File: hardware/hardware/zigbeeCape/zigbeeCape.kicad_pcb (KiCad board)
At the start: 4 copper layers, 63.5 x 54.6 mm, 80 parts, among them J1 Conn_ARM_JTAG_SWD_10, SW1 SW_MEC_5E, SW2 SW_MEC_5E, SW3 SW_MEC_5E, SW4 SW_MEC_5E, SW5 SW_MEC_5E, U1 CC1352R, U2 0.8Ghz_and_2.4GHz_Filter, U3 SMA_Antenna, U4 BeagleBone_P8, U5 BeagleBone_P9, Y1 32.768kHz, Y2 48MHz

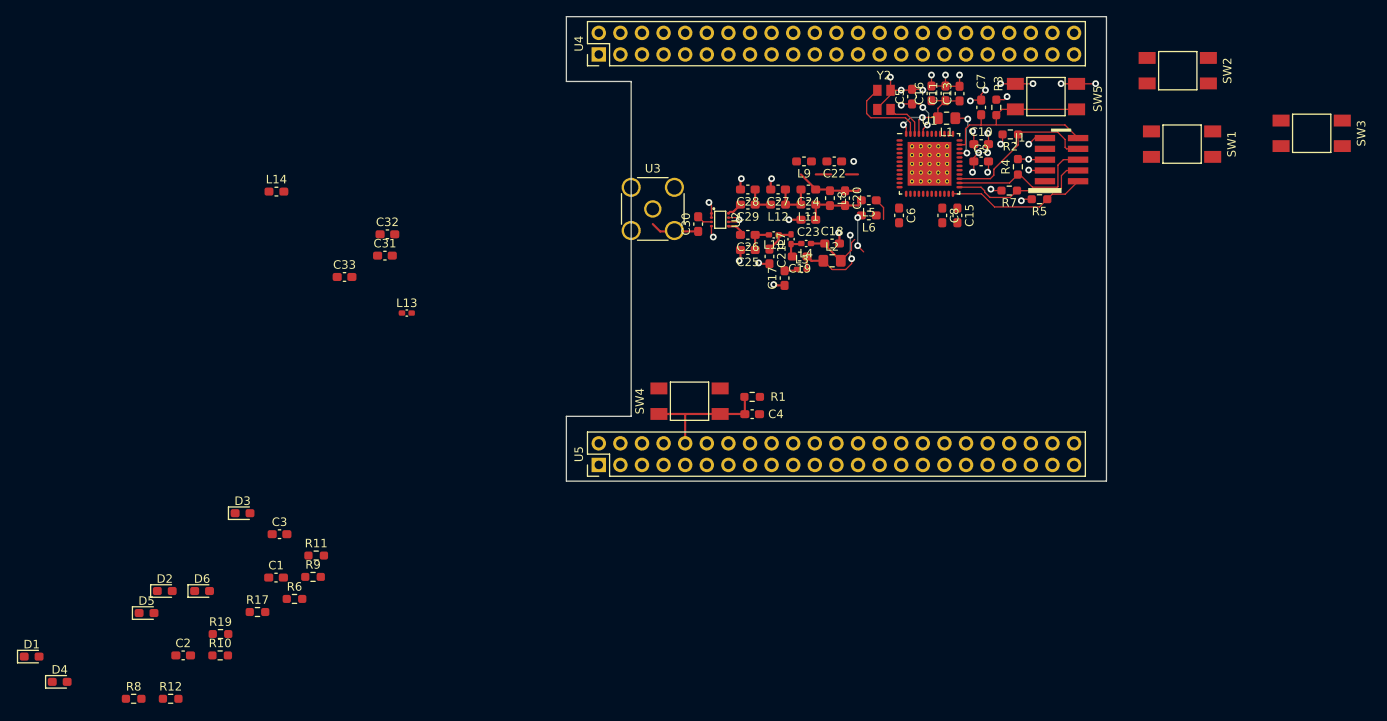
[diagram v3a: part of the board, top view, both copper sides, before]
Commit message: Buttons, most LEDs are done
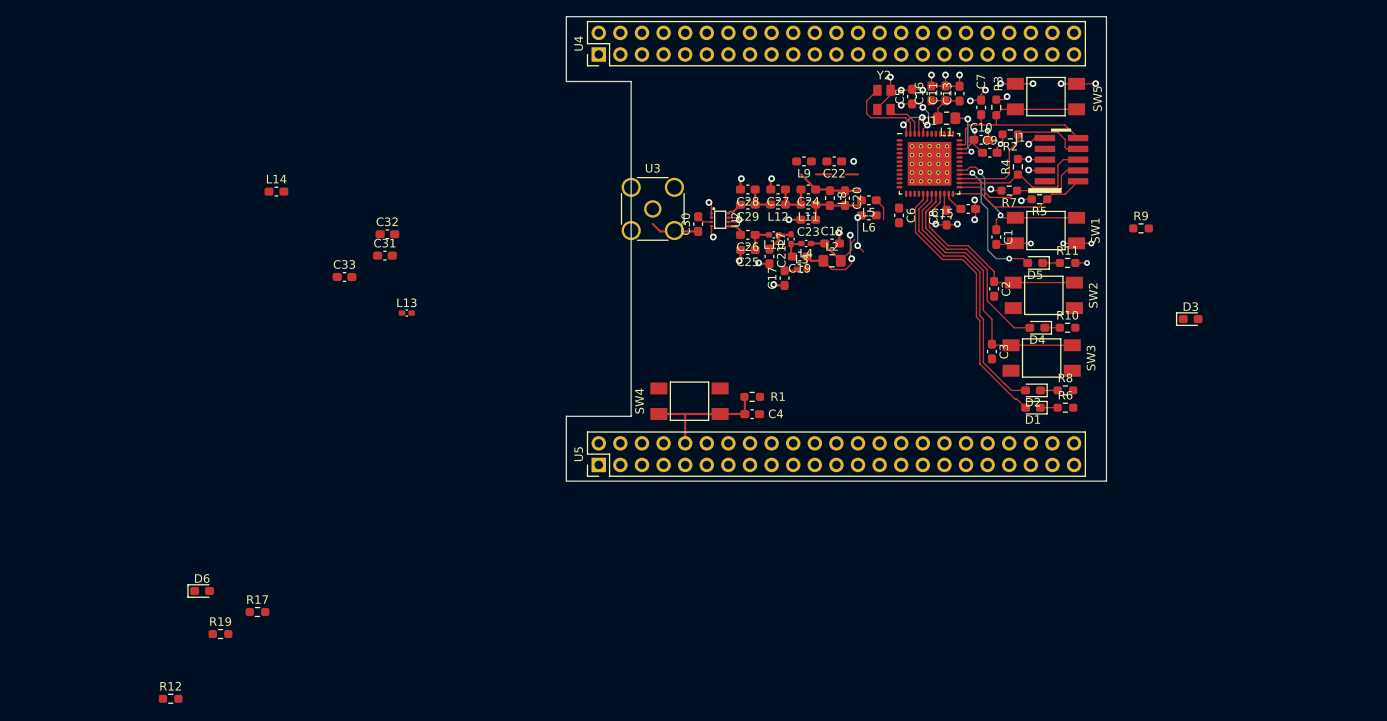
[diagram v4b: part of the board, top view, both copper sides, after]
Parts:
- moved D4 122.3 mm to (55.4, -18.0), turned to 180 degrees
- moved D1 121.3 mm to (54.9, -8.64), turned to 180 degrees
- moved R8 115.4 mm to (58.7, -10.7)
- moved D3 113.8 mm to (73.4, -19.1)
- moved D5 112.3 mm to (55.1, -25.7), turned to 180 degrees
- moved R10 106.8 mm to (58.9, -18.0)
- moved R9 105.6 mm to (67.6, -29.7)
- moved D2 104.8 mm to (54.9, -10.7), turned to 180 degrees
- moved C2 104.6 mm to (50.3, -22.6), turned to 270 degrees
- moved R11 94.8 mm to (58.9, -25.7)
- moved C1 93.7 mm to (50.5, -28.7), turned to 270 degrees
- moved R6 93.4 mm to (58.7, -8.64)
- moved C3 86.5 mm to (50.0, -15.2), turned to 270 degrees
- moved SW3 41.3 mm to (55.9, -14.5)
- moved SW2 30.8 mm to (56.1, -21.8)
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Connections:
- C4 pad 1: /BeagleBone_Headers/BeagleBone_Reset -> Net-(C4-Pad1)
- R1 pad 2: /BeagleBone_Headers/BeagleBone_Reset -> Net-(C4-Pad1)
- R17 pad 2: I2C2_SDA -> I2C2_SCL
- R19 pad 2: I2C2_SCL -> I2C2_SDA
- SW4 pad 3: /BeagleBone_Headers/BeagleBone_Reset -> Net-(C4-Pad1)
- SW4 pad 4: /BeagleBone_Headers/BeagleBone_Reset -> Net-(C4-Pad1)
- U1 pad 15: Net-(U1-Pad15) -> I2C2_SCL
- U1 pad 16: Net-(U1-Pad16) -> I2C2_SDA
- U1 pad 17: Net-(U1-Pad17) -> Aux_1
- U1 pad 18: Net-(U1-Pad18) -> Aux_2
- U1 pad 19: Net-(U1-Pad19) -> Check_Error
- U1 pad 20: I2C2_SCL -> ZigBee_HeartBeat
- U1 pad 21: I2C2_SDA -> ZigBee_Connect
- U1 pad 28: ZigBee_Connect -> Lan_HeartBeat
- U1 pad 29: Check_Error -> Network_Connect
- U1 pad 30: ZigBee_HeartBeat -> Net-(U1-Pad30)
- U1 pad 31: Cape_HeartBeat -> Net-(U1-Pad31)
- U1 pad 32: Aux_2 -> Net-(U1-Pad32)
- U1 pad 36: Aux_1 -> Net-(U1-Pad36)
- U1 pad 37: Net-(U1-Pad37) -> Cape_HeartBeat
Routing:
- net Aux_1: track 0.00 -> 32.4 mm
- net Check_Error: track 0.00 -> 32.4 mm
- net Aux_2: track 0.00 -> 31.1 mm
- net ZigBee_Connect: track 0.00 -> 24.9 mm
- net ZigBee_HeartBeat: track 0.00 -> 23.8 mm
- net Network_Connect: track 0.00 -> 19.9 mm, vias 0 -> 2
- net Lan_HeartBeat: track 0.00 -> 16.8 mm, vias 0 -> 2
- net GND: track 58.8 -> 72.9 mm, vias 32 -> 38
- net Net-(C15-Pad1): track 0.00 -> 2.48 mm
- net Net-(D5-Pad1): track 0.00 -> 2.02 mm
- net Net-(D2-Pad1): track 0.00 -> 2.02 mm
- net Net-(D1-Pad1): track 0.00 -> 2.02 mm
- net Net-(D4-Pad1): track 0.00 -> 1.77 mm
- net +3V3: track 13.8 -> 15.0 mm, vias 7 -> 5
- net Net-(J1-Pad8): track 19.1 -> 20.1 mm
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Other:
- rule via_min_drill: 0.3 -> 0.3302
- rule via_min_size: 0.4 -> 0.6858

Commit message: Setup DRC, completed coms lines
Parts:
- moved R19 87.7 mm to (38.1, -20.6), turned to 90 degrees
- moved R17 84.6 mm to (38.1, -24.9), turned to 90 degrees
- moved C26 46.1 mm to (-23.1, -41.1)
- moved L10 46.1 mm to (-20.1, -41.1)
- moved L3 46.1 mm to (-16.8, -37.1)
- moved C17 46.1 mm to (-18.8, -36.1)
- moved C18 46.1 mm to (-13.2, -40.1)
- moved C19 46.1 mm to (-17.0, -38.6)
- moved C21 46.1 mm to (-20.6, -38.6)
- moved C22 46.1 mm to (-13.0, -49.8)
- moved C23 46.1 mm to (-16.0, -42.9)
- moved C24 46.1 mm to (-16.0, -46.5)
- moved C25 46.1 mm to (-23.1, -39.4)
- moved C27 46.1 mm to (-19.6, -46.5)
- moved C28 46.1 mm to (-23.1, -46.5)
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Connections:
- C4 pad 1: Net-(C4-Pad1) -> /BeagleBone_Headers/BeagleBone_Reset
- R1 pad 2: Net-(C4-Pad1) -> /BeagleBone_Headers/BeagleBone_Reset
- SW4 pad 3: Net-(C4-Pad1) -> /BeagleBone_Headers/BeagleBone_Reset
- SW4 pad 4: Net-(C4-Pad1) -> /BeagleBone_Headers/BeagleBone_Reset
- U1 pad 10: SPI_MISO -> I2C2_SDA
- U1 pad 11: SPI_MOSI -> I2C2_SCL
- U1 pad 12: SPI_CS -> SPI_CLK
- U1 pad 14: SPI_CLK -> SPI_MISO
- U1 pad 15: I2C2_SCL -> UART_TX
- U1 pad 16: I2C2_SDA -> UART_RX
- U1 pad 31: Net-(U1-Pad31) -> Cape_HeartBeat
- U1 pad 37: Cape_HeartBeat -> Net-(U1-Pad37)
- U1 pad 8: UART_RX -> SPI_MOSI
- U1 pad 9: UART_TX -> SPI_CS
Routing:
- net I2C2_SCL: track 0.00 -> 43.6 mm
- net SPI_CS: track 0.00 -> 41.2 mm
- net I2C2_SDA: track 0.00 -> 39.6 mm
- net SPI_MOSI: track 0.00 -> 39.2 mm
- net GND: track 72.9 -> 112.1 mm, vias 38 -> 62
- net SPI_CLK: track 0.00 -> 37.8 mm
- net SPI_MISO: track 0.00 -> 36.5 mm
- net UART_TX: track 0.00 -> 33.2 mm
- net UART_RX: track 0.00 -> 32.3 mm
- net Cape_HeartBeat: track 0.00 -> 9.56 mm, vias 0 -> 2
- net +3V3: track 15.0 -> 23.1 mm, vias 5 -> 10
- net Net-(C14-Pad1): track 0.00 -> 6.54 mm
- net Net-(C12-Pad1): track 0.00 -> 6.02 mm
- net Net-(D3-Pad1): track 0.00 -> 2.78 mm
- net Net-(C15-Pad1): track 2.48 -> 3.44 mm
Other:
- net class Default: clearance 0.254 -> 0.1524
- rule trace_clearance: 0.254 -> 0.1524

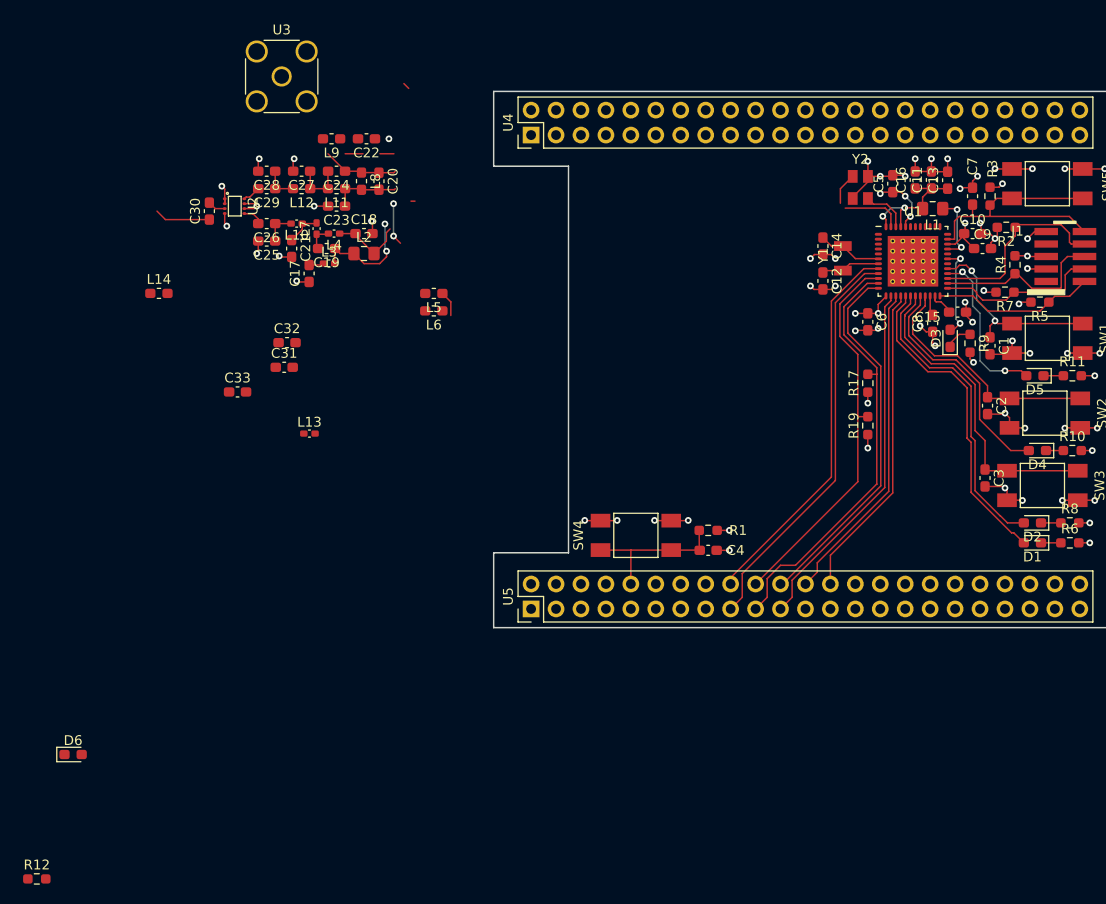
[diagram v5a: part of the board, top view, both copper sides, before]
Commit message: Finished ZigBee circuit, Removed PCB antenna
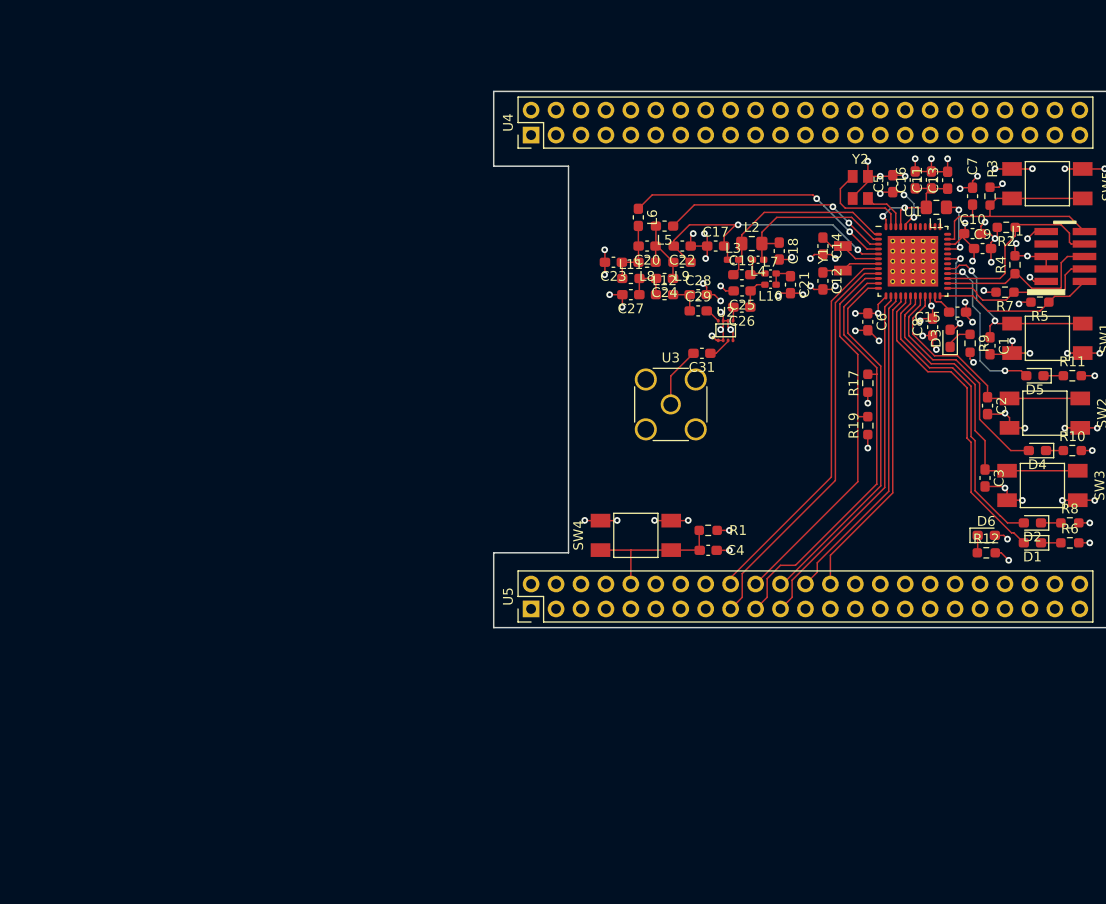
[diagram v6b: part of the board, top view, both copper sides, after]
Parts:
- removed C30, C32: DNM, Capacitor_SMD:C_0603_1608Metric_Pad1.08x0.95mm_HandSolder
- removed C33: 5.6pF, Capacitor_SMD:C_0603_1608Metric_Pad1.08x0.95mm_HandSolder
- removed L13: 3.3nH, Inductor_SMD:L_0402_1005Metric_Pad0.77x0.64mm_HandSolder
- removed L14: DNM, Inductor_SMD:L_0603_1608Metric_Pad1.05x0.95mm_HandSolder
- moved R12 102.2 mm to (50.2, -7.62)
- moved D6 95.6 mm to (50.2, -9.40)
- moved U3 51.8 mm to (18.0, -22.7)
- moved U2 51.6 mm to (23.6, -30.2), turned to 0 degrees
- moved C21 50.9 mm to (30.2, -34.9)
- moved C26 49.1 mm to (25.3, -32.6)
- moved C25 48.7 mm to (25.3, -34.3)
- moved L10 48.7 mm to (28.2, -34.9)
- moved L7 46.5 mm to (28.2, -36.1), turned to 0 degrees
- moved C28 45.7 mm to (20.8, -33.9), turned to 0 degrees
- moved C29 45.7 mm to (20.8, -32.3), turned to 0 degrees
- moved L4 43.3 mm to (26.9, -37.5)
- moved C31 42.6 mm to (21.2, -27.9), turned to 180 degrees
- moved C19 42.4 mm to (25.3, -35.9), turned to 0 degrees
- moved C18 42.3 mm to (29.1, -38.4), turned to 270 degrees
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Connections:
- C31 pad 2: Net-(C30-Pad2) -> Net-(C31-Pad2)
- U2 pad 3: Net-(C30-Pad2) -> Net-(C31-Pad1)
- U3 pad 1: Net-(C30-Pad1) -> Net-(C31-Pad2)
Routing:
- net /ZigBeeFiltering/SUB-1_GHZ_RF_N: track 0.41 -> 27.3 mm, vias 0 -> 2
- net /ZigBeeFiltering/RX_TX: track 3.34 -> 30.1 mm, vias 0 -> 2
- net /ZigBeeFiltering/SUB-1_GHZ_RF_P: track 2.60 -> 23.5 mm, vias 0 -> 2
- net GND: track 112.1 -> 125.5 mm, vias 62 -> 70
- net /ZigBeeFiltering/2_4_GHZ_RF_N: track 7.61 -> 18.1 mm
- net /ZigBeeFiltering/2_4_GHZ_RF_P: track 11.1 -> 20.2 mm, vias 2 -> 0
- net +3V3: track 23.1 -> 29.8 mm, vias 10 -> 15
- net Net-(C31-Pad2): track 0.00 -> 6.16 mm
- net Net-(C30-Pad1): track 5.69 -> 0.00 mm
- net Net-(C20-Pad2): track 11.3 -> 7.07 mm, vias 2 -> 0
- net Net-(C31-Pad1): track 0.00 -> 2.39 mm
- net Net-(C30-Pad2): track 1.82 -> 0.00 mm
- net Net-(D6-Pad1): track 0.00 -> 1.79 mm
- net Net-(C21-Pad1): track 3.61 -> 2.72 mm
- net Net-(C26-Pad2): track 2.11 -> 1.40 mm

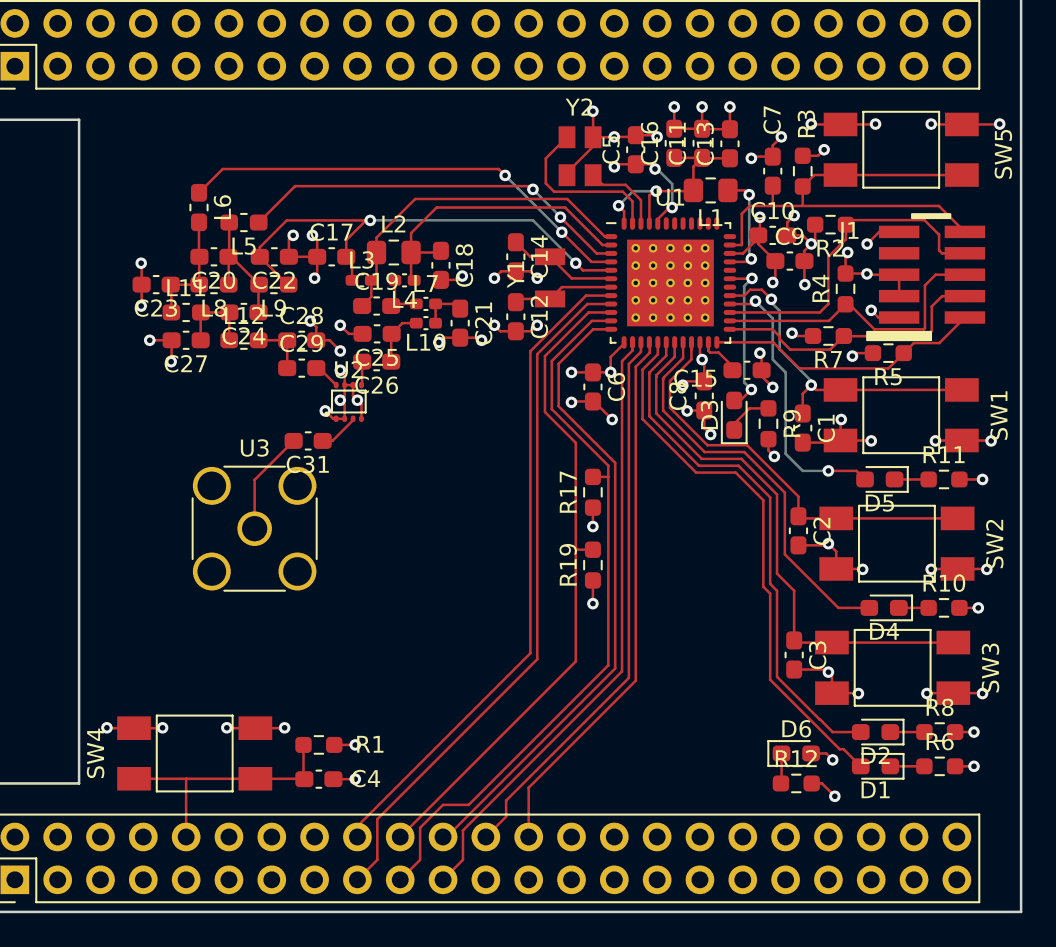
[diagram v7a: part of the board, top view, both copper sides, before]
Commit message: Changed min via size, rerouted lan/wifi, cleaned up traces
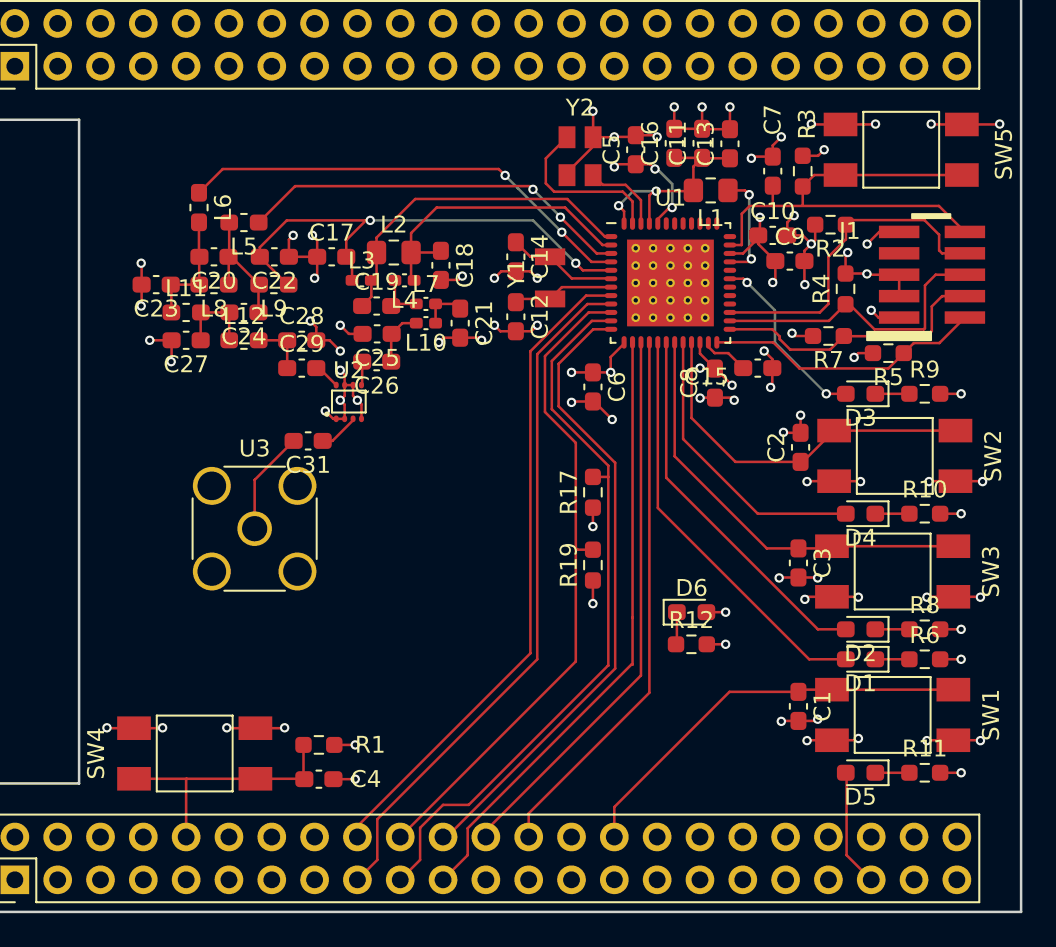
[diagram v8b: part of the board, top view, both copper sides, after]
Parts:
- moved SW1 17.8 mm to (55.9, -11.7)
- moved D5 17.4 mm to (54.0, -8.26)
- moved R11 17.4 mm to (57.8, -8.26)
- moved C1 16.5 mm to (50.3, -12.2)
- moved D6 10.4 mm to (44.0, -17.8)
- moved R12 10.3 mm to (43.9, -15.9)
- moved R9 9.44 mm to (57.8, -30.7), turned to 0 degrees
- moved D3 7.60 mm to (54.0, -30.7), turned to 180 degrees
- moved R6 6.41 mm to (57.8, -15.0)
- moved D1 6.41 mm to (54.0, -15.0)
- moved R8 6.16 mm to (57.8, -16.8)
- moved D2 6.16 mm to (54.0, -16.8)
- moved D4 5.76 mm to (54.0, -23.6)
- moved SW3 5.72 mm to (55.9, -20.2)
- moved R10 5.70 mm to (57.8, -23.6)
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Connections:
- U1 pad 28: Lan_HeartBeat -> Net-(U1-Pad28)
- U1 pad 29: Network_Connect -> Net-(U1-Pad29)
- U1 pad 49: (no net) -> GND
- U5 pad 15: Network_Connect -> Net-(U5-Pad15)
- U5 pad 30: Net-(U5-Pad30) -> Network_Connect
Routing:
- net Lan_HeartBeat: track 16.8 -> 6.98 mm, vias 2 -> 0
- net Aux_2: track 31.1 -> 22.4 mm
- net Aux_1: track 32.4 -> 24.7 mm
- net Check_Error: track 32.4 -> 25.6 mm
- net ZigBee_HeartBeat: track 23.8 -> 17.2 mm
- net Network_Connect: track 19.9 -> 24.8 mm, vias 2 -> 0
- net ZigBee_Connect: track 24.9 -> 22.0 mm
- net Cape_HeartBeat: track 9.56 -> 10.8 mm
- net Net-(D3-Pad1): track 2.78 -> 2.02 mm
- net Net-(C15-Pad1): track 3.44 -> 2.85 mm
- net GND: track 125.5 -> 125.0 mm, vias 70 -> 76
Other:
- net class Default: via_dia 0.8 -> 0.5588; via_drill 0.4 -> 0.3048
- rule via_min_drill: 0.3302 -> 0.3048
- rule via_min_size: 0.6858 -> 0.5588
